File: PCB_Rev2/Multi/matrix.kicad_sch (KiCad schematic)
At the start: 141 parts

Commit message: Update matrix.kicad_sch
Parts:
- S1, S10, S11, S12, S13, S14-2, S16, S17, S18, S19, S2, S20, S21, S22, S23, S24, S25, S26, S27, S3, S30, S31, S32, S33, S34, S35, S36, S37, S38, S39, S4, S40, S41, S42, S43, S45, S46, S47, S48, S49, S5, S50, S51, S52, S54, S56, S58-2, S6, S63-2, S7, S8, S9: footprint PCM_Switch_Keyboard_Hotswap_Kailh:SW_Hotswap_Kailh_MX_Plated_1.00u -> PCM_Switch_Keyboard_Hotswap_Kailh:SW_Hotswap_Kailh_MX_plated_1.00u
- S14: footprint PCM_Switch_Keyboard_Hotswap_Kailh:SW_Hotswap_Kailh_MX_Plated_2.00u -> PCM_Switch_Keyboard_Hotswap_Kailh:SW_Hotswap_Kailh_MX_plated_2.00u
- S15: footprint PCM_Switch_Keyboard_Hotswap_Kailh:SW_Hotswap_Kailh_MX_Plated_1.50u -> PCM_Switch_Keyboard_Hotswap_Kailh:SW_Hotswap_Kailh_MX_plated_1.50u
- S28: footprint PCM_Switch_Keyboard_Hotswap_Kailh:SW_Hotswap_Kailh_MX_Plated_ISOEnter_90deg -> PCM_Switch_Keyboard_Hotswap_Kailh:SW_Hotswap_Kailh_MX_plated_ISOEnter_90deg
- S28-2: footprint PCM_Switch_Keyboard_Hotswap_Kailh:SW_Hotswap_Kailh_MX_Plated_2.25u_90deg -> PCM_Switch_Keyboard_Hotswap_Kailh:SW_Hotswap_Kailh_MX_plated_2.25u_90deg
- S29, S55: footprint PCM_Switch_Keyboard_Hotswap_Kailh:SW_Hotswap_Kailh_MX_Plated_1.75u_90deg -> PCM_Switch_Keyboard_Hotswap_Kailh:SW_Hotswap_Kailh_MX_plated_1.75u_90deg
- S29-2, S55, S56, S57, S60, S61, S62: footprint PCM_Switch_Keyboard_Hotswap_Kailh:SW_Hotswap_Kailh_MX_Plated_1.25u_90deg -> PCM_Switch_Keyboard_Hotswap_Kailh:SW_Hotswap_Kailh_MX_plated_1.25u_90deg
- S41-2, S57-2, S59-2, S62-2, S64-2: footprint PCM_Switch_Keyboard_Hotswap_Kailh:SW_Hotswap_Kailh_MX_Plated_1.50u_90deg -> PCM_Switch_Keyboard_Hotswap_Kailh:SW_Hotswap_Kailh_MX_plated_1.50u_90deg
- S42, S59: footprint PCM_Switch_Keyboard_Hotswap_Kailh:SW_Hotswap_Kailh_MX_Plated_1.25u -> PCM_Switch_Keyboard_Hotswap_Kailh:SW_Hotswap_Kailh_MX_plated_1.25u
- S43-2: footprint PCM_Switch_Keyboard_Hotswap_Kailh:SW_Hotswap_Kailh_MX_Plated_2.25u -> PCM_Switch_Keyboard_Hotswap_Kailh:SW_Hotswap_Kailh_MX_plated_2.25u
- S55-2: footprint PCM_Switch_Keyboard_Hotswap_Kailh:SW_Hotswap_Kailh_MX_Plated_2.75u_90deg -> PCM_Switch_Keyboard_Hotswap_Kailh:SW_Hotswap_Kailh_MX_plated_2.75u_90deg
- S58: footprint PCM_Switch_Keyboard_Hotswap_Kailh:SW_Hotswap_Kailh_MX_Plated_6.25u -> PCM_Switch_Keyboard_Hotswap_Kailh:SW_Hotswap_Kailh_MX_plated_6.25u
- S60-2: footprint PCM_Switch_Keyboard_Hotswap_Kailh:SW_Hotswap_Kailh_MX_Plated_7.00u -> PCM_Switch_Keyboard_Hotswap_Kailh:SW_Hotswap_Kailh_MX_plated_7.00u

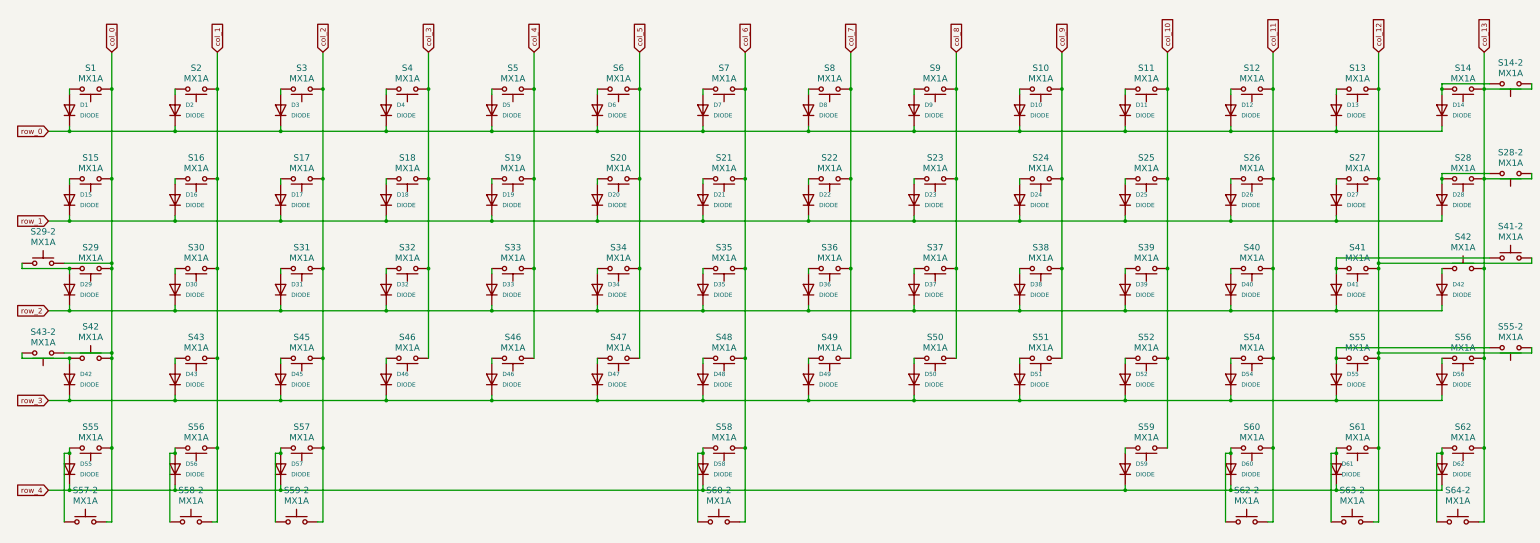
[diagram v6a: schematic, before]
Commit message: Adjust Switch Direction
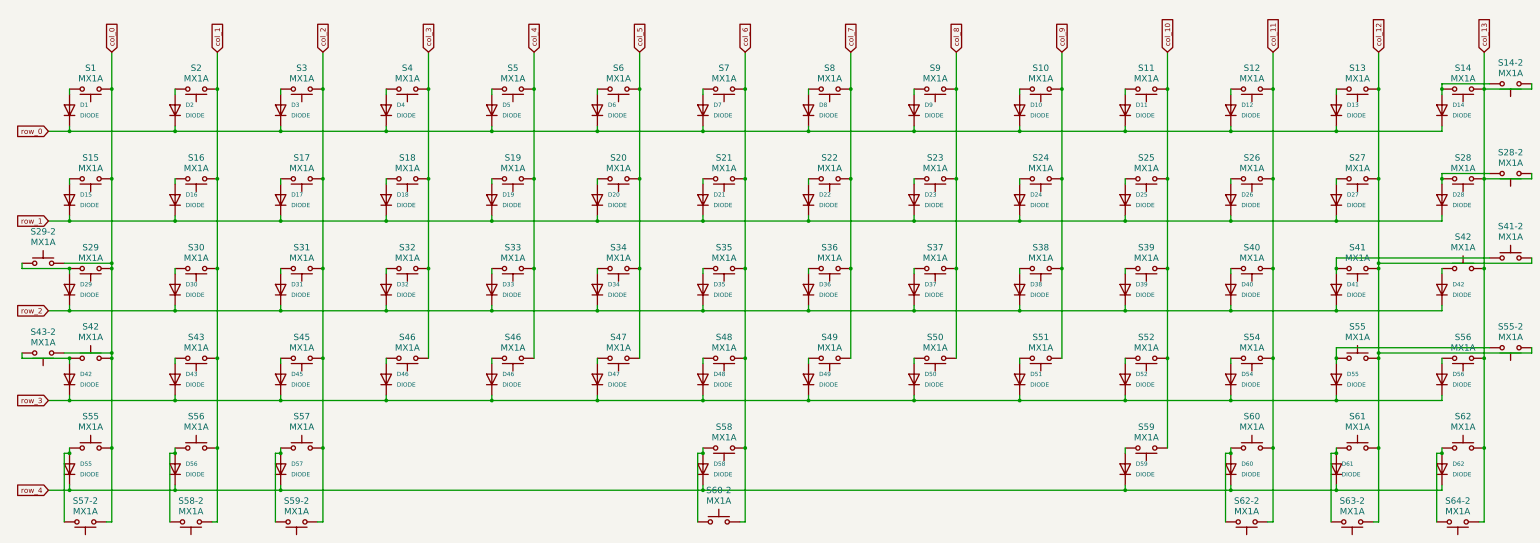
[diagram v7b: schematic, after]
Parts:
- S29: footprint PCM_Switch_Keyboard_Hotswap_Kailh:SW_Hotswap_Kailh_MX_plated_1.75u_90deg -> PCM_Switch_Keyboard_Hotswap_Kailh:SW_Hotswap_Kailh_MX_plated_1.75u
- S29-2, S55, S56, S57, S60, S61, S62: footprint PCM_Switch_Keyboard_Hotswap_Kailh:SW_Hotswap_Kailh_MX_plated_1.25u_90deg -> PCM_Switch_Keyboard_Hotswap_Kailh:SW_Hotswap_Kailh_MX_plated_1.25u
- S57-2, S59-2, S62-2, S64-2: footprint PCM_Switch_Keyboard_Hotswap_Kailh:SW_Hotswap_Kailh_MX_plated_1.50u_90deg -> PCM_Switch_Keyboard_Hotswap_Kailh:SW_Hotswap_Kailh_MX_plated_1.50u
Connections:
- net col_0: now also S55.1, S57-2.2; no longer S55.2, S57-2.1
- net col_1: now also S56.1, S58-2.2; no longer S56.2, S58-2.1
- net col_11: now also S60.1, S62-2.2; no longer S60.2, S62-2.1
- net col_12: now also S55.1, S61.1, S63-2.2; no longer S55.2, S61.2, S63-2.1
- net col_13: now also S62.1, S64-2.2; no longer S62.2, S64-2.1
- net col_2: now also S57.1, S59-2.2; no longer S57.2, S59-2.1
- net at D55.2 (A), S55-2.1: now also S55.2; no longer S55.1
- new net: D62.2 (A), S62.2, S64-2.1
- new net: D56.2 (A), S56.2, S58-2.1
- new net: D60.2 (A), S60.2, S62-2.1
- new net: D57.2 (A), S57.2, S59-2.1
- new net: D61.2 (A), S61.2, S63-2.1
- new net: D55.2 (A), S55.2, S57-2.1
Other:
- moved on the sheet: S55, S56, S57, S57-2, S58-2, S59-2, S60, S61, S62, S62-2, S63-2, S64-2

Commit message: QFN-56 Thermal Via Redesign
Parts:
- S1, S10, S11, S12, S13, S14-2, S16, S17, S18, S19, S2, S20, S21, S22, S23, S24, S25, S26, S27, S3, S30, S31, S32, S33, S34, S35, S36, S37, S38, S39, S4, S40, S41, S42, S43, S45, S46, S47, S48, S49, S5, S50, S51, S52, S54, S56, S58-2, S6, S63-2, S7, S8, S9: footprint PCM_Switch_Keyboard_Hotswap_Kailh:SW_Hotswap_Kailh_MX_plated_1.00u -> PCM_Switch_Keyboard_Hotswap_Kailh:SW_Hotswap_Kailh_MX_Plated_1.00u
- S14: footprint PCM_Switch_Keyboard_Hotswap_Kailh:SW_Hotswap_Kailh_MX_plated_2.00u -> PCM_Switch_Keyboard_Hotswap_Kailh:SW_Hotswap_Kailh_MX_Plated_2.00u
- S15, S57-2, S59-2, S62-2, S64-2: footprint PCM_Switch_Keyboard_Hotswap_Kailh:SW_Hotswap_Kailh_MX_plated_1.50u -> PCM_Switch_Keyboard_Hotswap_Kailh:SW_Hotswap_Kailh_MX_Plated_1.50u
- S28: footprint PCM_Switch_Keyboard_Hotswap_Kailh:SW_Hotswap_Kailh_MX_plated_ISOEnter_90deg -> PCM_Switch_Keyboard_Hotswap_Kailh:SW_Hotswap_Kailh_MX_Plated_ISOEnter_90deg
- S28-2: footprint PCM_Switch_Keyboard_Hotswap_Kailh:SW_Hotswap_Kailh_MX_plated_2.25u_90deg -> PCM_Switch_Keyboard_Hotswap_Kailh:SW_Hotswap_Kailh_MX_Plated_2.25u_90deg
- S29: footprint PCM_Switch_Keyboard_Hotswap_Kailh:SW_Hotswap_Kailh_MX_plated_1.75u -> PCM_Switch_Keyboard_Hotswap_Kailh:SW_Hotswap_Kailh_MX_Plated_1.75u
- S29-2, S42, S55, S56, S57, S59, S60, S61, S62: footprint PCM_Switch_Keyboard_Hotswap_Kailh:SW_Hotswap_Kailh_MX_plated_1.25u -> PCM_Switch_Keyboard_Hotswap_Kailh:SW_Hotswap_Kailh_MX_Plated_1.25u
- S41-2: footprint PCM_Switch_Keyboard_Hotswap_Kailh:SW_Hotswap_Kailh_MX_plated_1.50u_90deg -> PCM_Switch_Keyboard_Hotswap_Kailh:SW_Hotswap_Kailh_MX_Plated_1.50u_90deg
- S43-2: footprint PCM_Switch_Keyboard_Hotswap_Kailh:SW_Hotswap_Kailh_MX_plated_2.25u -> PCM_Switch_Keyboard_Hotswap_Kailh:SW_Hotswap_Kailh_MX_Plated_2.25u
- S55: footprint PCM_Switch_Keyboard_Hotswap_Kailh:SW_Hotswap_Kailh_MX_plated_1.75u_90deg -> PCM_Switch_Keyboard_Hotswap_Kailh:SW_Hotswap_Kailh_MX_Plated_1.75u
- S55-2: footprint PCM_Switch_Keyboard_Hotswap_Kailh:SW_Hotswap_Kailh_MX_plated_2.75u_90deg -> PCM_Switch_Keyboard_Hotswap_Kailh:SW_Hotswap_Kailh_MX_Plated_2.75u
- S58: footprint PCM_Switch_Keyboard_Hotswap_Kailh:SW_Hotswap_Kailh_MX_plated_6.25u -> PCM_Switch_Keyboard_Hotswap_Kailh:SW_Hotswap_Kailh_MX_Plated_6.25u
- S60-2: footprint PCM_Switch_Keyboard_Hotswap_Kailh:SW_Hotswap_Kailh_MX_plated_7.00u -> PCM_Switch_Keyboard_Hotswap_Kailh:SW_Hotswap_Kailh_MX_Plated_7.00u
